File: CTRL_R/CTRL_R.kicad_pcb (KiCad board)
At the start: 2 copper layers, 33.4 x 88 mm, 26 parts, among them J1 BM14B-NSHSS-TBT_LF__SN_, J2 BM04B-NSHSS-TBT_LF__SN_, J3 5051100592, U2 74LVC1G08

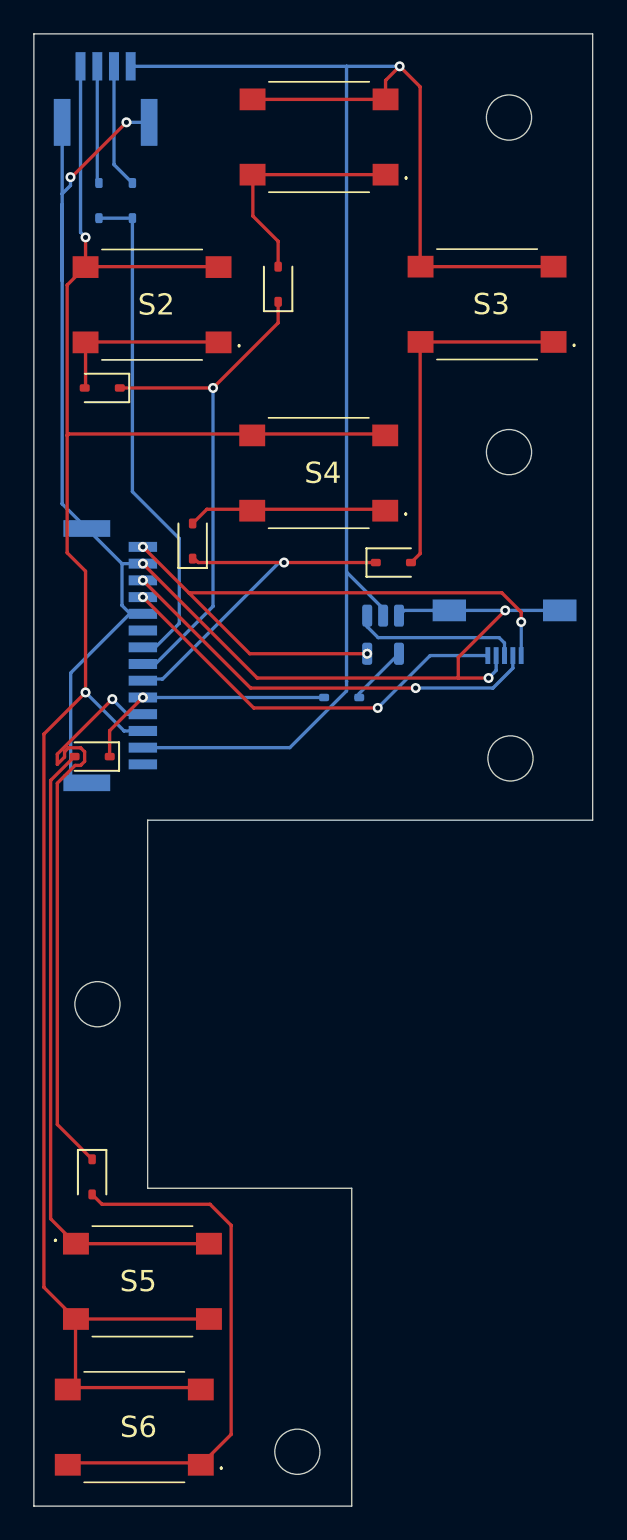
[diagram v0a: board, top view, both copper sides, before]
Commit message: Organized /3D Models
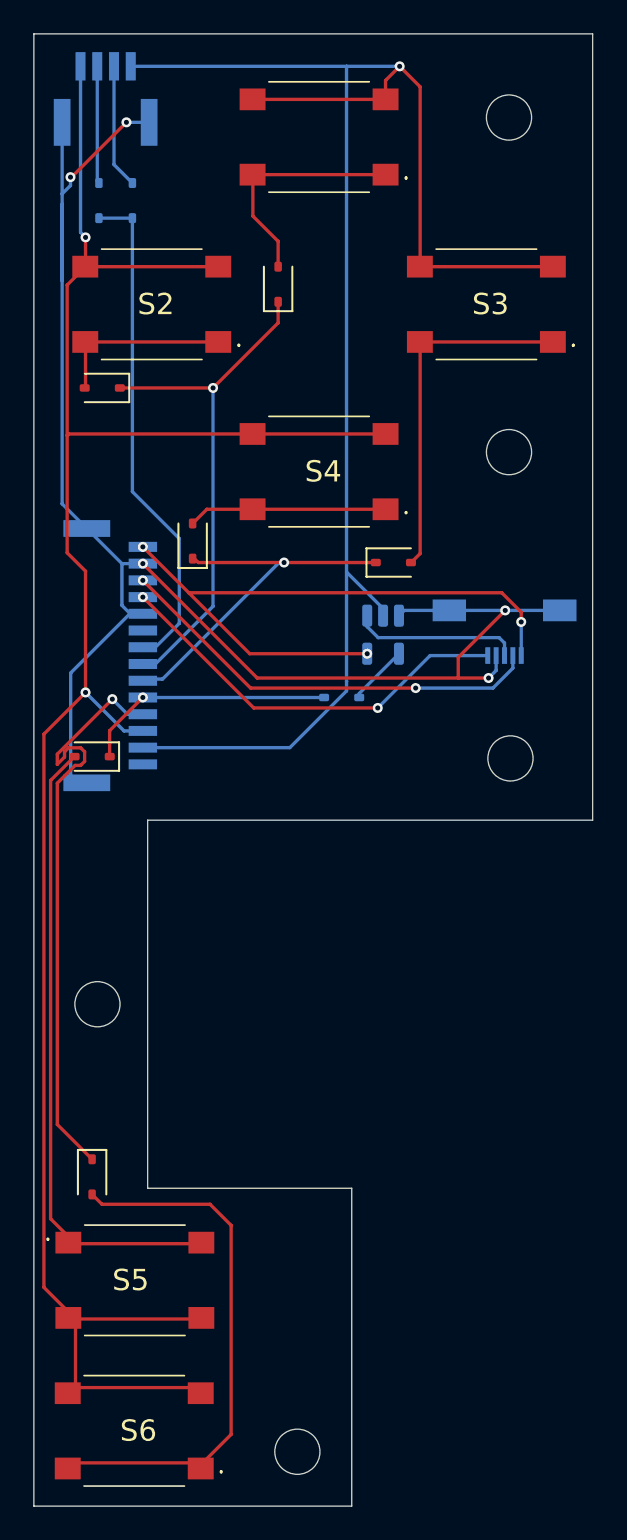
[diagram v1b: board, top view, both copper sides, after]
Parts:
- moved S5 0.46 mm to (83.6, 137.1)
- moved S6 0.22 mm to (83.6, 146.1)
- moved S4 0.09 mm to (94.6, 88.8)
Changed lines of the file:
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@@
 	(footprint "B3S-1000:B3S1000"
 		(layer "F.Cu")
-		(at 84.665 78.79)
+		(at 84.646462 78.764756)
 		(descr "B3S-1000-1")
 		(tags "Switch")
@@
 	(footprint "B3S-1000:B3S1000"
 		(layer "F.Cu")
-		(at 104.688962 78.764756)
+		(at 104.646462 78.764756)
 		(descr "B3S-1000-1")
 		(tags "Switch")
@@
 	(footprint "B3S-1000:B3S1000"
 		(layer "F.Cu")
-		(at 84.088962 137.164756 180)
+		(at 83.636 137.1 180)
 		(descr "B3S-1000-1")
 		(tags "Switch")
@@
 	(footprint "B3S-1000:B3S1000"
 		(layer "F.Cu")
-		(at 94.625 88.85)
+		(at 94.646462 88.764756)
 		(descr "B3S-1000-1")
 		(tags "Switch")
@@
 	(footprint "B3S-1000:B3S1000"
 		(layer "F.Cu")
-		(at 83.603 145.879)
+		(at 83.6 146.1)
 		(descr "B3S-1000-1")
 		(tags "Switch")
@@
 		(layer "B.SilkS")
 	)
+	(gr_circle
+		(center 94.646462 78.764756)
+		(end 104.646462 78.764756)
+		(stroke
+			(width 0.2)
+			(type solid)
+		)
+		(fill no)
+		(layer "Dwgs.User")
+	)
 	(gr_line
